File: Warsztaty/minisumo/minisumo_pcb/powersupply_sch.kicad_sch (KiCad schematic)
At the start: 7 parts, among them J1 Conn_01x02_Pin, U3 LM1117S-5.0, U8 LM1117S-3.3

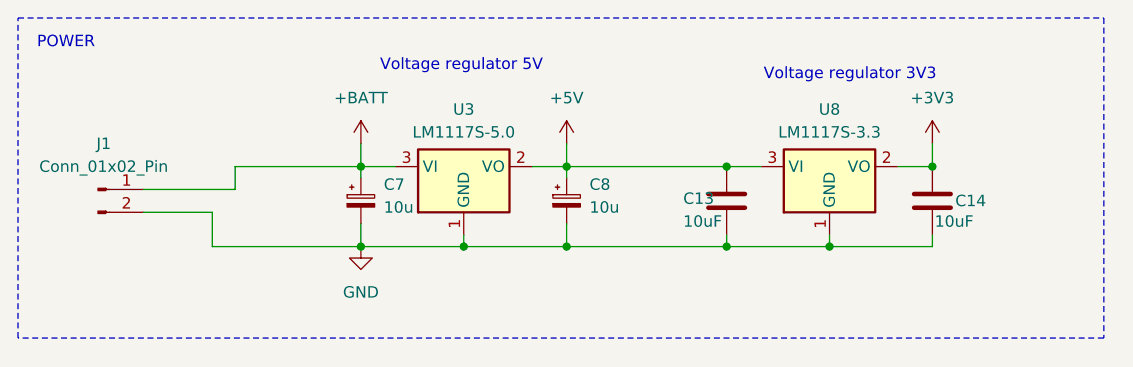
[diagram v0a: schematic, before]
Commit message: laczenie hierarchiczne schematu
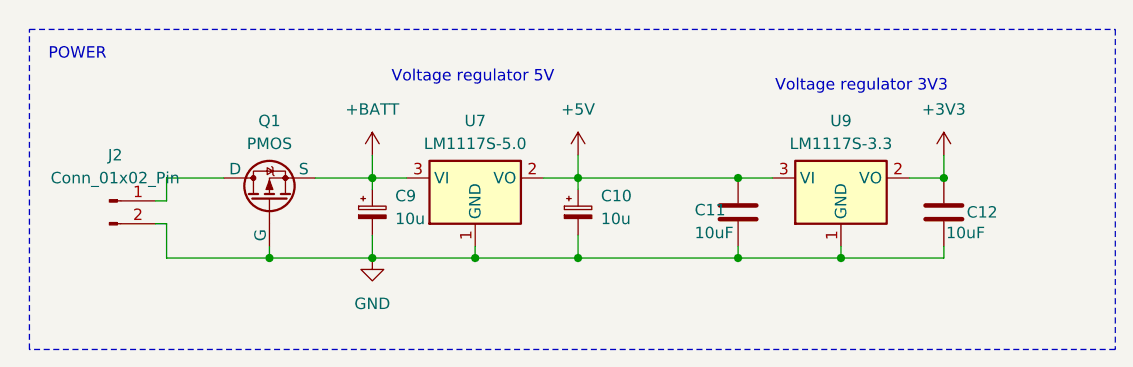
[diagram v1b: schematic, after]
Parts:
- removed C13, C14: 10uF, symbol Device:C
- removed C7, C8: 10u, symbol Device:C_Polarized_Small
- removed J1: Conn_01x02_Pin, symbol Connector:Conn_01x02_Pin
- removed U3: LM1117S-5.0, Package_TO_SOT_SMD:TO-263-3_TabPin2, symbol Regulator_Linear:LM1117S-5.0
- removed U8: LM1117S-3.3, Package_TO_SOT_SMD:TO-263-3_TabPin2, symbol Regulator_Linear:LM1117S-3.3
- added C10, C9: 10u, symbol Device:C_Polarized_Small
- added C11, C12: 10uF, symbol Device:C
- added J2: Conn_01x02_Pin, symbol Connector:Conn_01x02_Pin
- added Q1: PMOS, symbol Simulation_SPICE:PMOS
- added U7: LM1117S-5.0, Package_TO_SOT_SMD:TO-263-3_TabPin2, symbol Regulator_Linear:LM1117S-5.0
- added U9: LM1117S-3.3, Package_TO_SOT_SMD:TO-263-3_TabPin2, symbol Regulator_Linear:LM1117S-3.3
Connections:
- net +3V3: now also C12.1, U9.2 (VO)
- net +5V: now also C10.1, C11.1, U7.2 (VO), U9.3 (VI)
- net +BATT: now also C9.1, Q1.3 (S), U7.3 (VI)
- net GND: now also C10.2, C11.2, C12.2, C9.2, J2.2 (Pin_2), Q1.2 (G), U7.1 (GND), U9.1 (GND)
- new net: J2.1 (Pin_1), Q1.1 (D)

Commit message: wstepnie skonczony schemat
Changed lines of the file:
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@@
+		)
+	)
+	(hierarchical_label "+5V"
+		(shape input)
+		(at 74.93 29.21 0)
+		(fields_autoplaced yes)
+		(effects
+			(font
+				(size 1.27 1.27)
+			)
+			(justify left)
 		)
 	)

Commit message: chyba gotowy schemat
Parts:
- removed J2: Conn_01x02_Pin, symbol Connector:Conn_01x02_Pin
- added J1: HTSW-102-08-L-S, HTSW-102-08-L-S:SAMTEC_HTSW-102-08-L-S, symbol HTSW-102-08-L-S:HTSW-102-08-L-S
- C10, C11, C12, C9: footprint (none) -> Capacitor_SMD:C_0805_2012Metric_Pad1.18x1.45mm_HandSolder
- Q1: footprint (none) -> Package_TO_SOT_SMD:SOT-23-3
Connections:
- net GND: now also J1.01
- net +: now reaches Q1.1 (D)
- net +: now also J1.02
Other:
- moved on the sheet: C10, C11, C12, C9, Q1, U7, U9

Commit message: chyba gotowy schemat
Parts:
- removed C11, C12: 10uF, Capacitor_SMD:C_0805_2012Metric_Pad1.18x1.45mm_HandSolder, symbol Device:C
- removed U9: LM1117S-3.3, Package_TO_SOT_SMD:TO-263-3_TabPin2, symbol Regulator_Linear:LM1117S-3.3
- C10, C9: footprint Capacitor_SMD:C_0805_2012Metric_Pad1.18x1.45mm_HandSolder -> Capacitor_Tantalum_SMD:CP_EIA-3528-12_Kemet-T
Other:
- note removed: "Voltage regulator 3V3"

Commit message: stan przed usunięciem jednego czujnika lini
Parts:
- added S1: 1101M2S3CQE2, 1101M2S3CQE2:SW_1101M2S3CQE2, symbol 1101M2S3CQE2:1101M2S3CQE2
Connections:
- net +: now also S1.2; no longer Q1.1 (D)
- new net: Q1.1 (D), S1.1
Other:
- moved on the sheet: Q1
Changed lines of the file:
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@@
 	)
 	(junction
-		(at 43.18 40.64)
+		(at 45.72 40.64)
 		(diameter 0)
 		(color 0 0 0 0)
@@
 	(wire
 		(pts
-			(xy 43.18 39.37) (xy 43.18 40.64)
-		)
-		(stroke
-			(width 0)
-			(type default)
-		)
-	)
-	(wire
-		(pts
-			(xy 43.18 40.64) (xy 31.75 40.64)
+			(xy 45.72 39.37) (xy 45.72 40.64)
+		)
+		(stroke
+			(width 0)
+			(type default)
+		)
+	)
+	(wire
+		(pts
+			(xy 31.75 40.64) (xy 45.72 40.64)
 		)
 		(stroke
@@
 	(wire
 		(pts
-			(xy 31.75 31.75) (xy 38.1 31.75)
+			(xy 40.64 29.21) (xy 40.64 31.75)
+		)
+		(stroke
+			(width 0)
+			(type default)
+		)
+	)
+	(wire
+		(pts
+			(xy 45.72 40.64) (xy 54.61 40.64)
 		)
 		(stroke
@@
 	(wire
 		(pts
-			(xy 48.26 31.75) (xy 54.61 31.75)
-		)
-		(stroke
-			(width 0)
-			(type default)
-		)
-	)
-	(wire
-		(pts
-			(xy 43.18 40.64) (xy 54.61 40.64)
+			(xy 50.8 31.75) (xy 54.61 31.75)
 		)
 		(stroke
@@
 		(pts
 			(xy 73.66 31.75) (xy 77.47 31.75)
+		)
+		(stroke
+			(width 0)
+			(type default)
+		)
+	)
+	(wire
+		(pts
+			(xy 39.37 29.21) (xy 40.64 29.21)
 		)
 		(stroke
@@
 		(effects
 			(font
-				(size 1.27 1.27)
+				(size 0.762 0.762)
 			)
 			(justify left)
 		)
 		(property "Intersheetrefs" "${INTERSHEET_REFS}"
-			(at 31.75 27.1924 90)
+			(at 31.75 29.0152 90)
 			(effects
 				(font
@@
 		)
 		(property "Value" "HTSW-102-08-L-S"
-			(at 37.084 25.654 0)
+			(at 34.798 41.656 0)
 			(effects
 				(font
@@
 	(symbol
 		(lib_id "Simulation_SPICE:PMOS")
-		(at 43.18 34.29 90)
+		(at 45.72 34.29 90)
 		(unit 1)
 		(exclude_from_sim no)
@@
 		(fields_autoplaced yes)
 		(property "Reference" "Q1"
-			(at 43.18 25.4 90)
+			(at 45.72 25.4 90)
 			(effects
 				(font
@@
 		)
 		(property "Value" "PMOS"
-			(at 43.18 27.94 90)
+			(at 45.72 27.94 90)
 			(effects
 				(font
@@
 		)
 		(property "Footprint" "Package_TO_SOT_SMD:SOT-23-3"
-			(at 40.64 29.21 0)
+			(at 43.18 29.21 0)
 			(effects
 				(font
@@
 		)
 		(property "Datasheet" "https://ngspice.sourceforge.io/docs/ngspice-html-manual/manual.xhtml#cha_MOSFETs"
-			(at 55.88 34.29 0)
+			(at 58.42 34.29 0)
 			(effects
 				(font
@@
 		)
 		(property "Description" "P-MOSFET transistor, drain/source/gate"
-			(at 43.18 34.29 0)
+			(at 45.72 34.29 0)
 			(effects
 				(font
@@
 		)
 		(property "Sim.Device" "PMOS"
-			(at 60.325 34.29 0)
+			(at 62.865 34.29 0)
 			(effects
 				(font
@@
 		)
 		(property "Sim.Type" "VDMOS"
-			(at 62.23 34.29 0)
+			(at 64.77 34.29 0)
 			(effects
 				(font
@@
 		)
 		(property "Sim.Pins" "1=D 2=G 3=S"
-			(at 58.42 34.29 0)
+			(at 60.96 34.29 0)
 			(effects
 				(font
@@
 					(unit 1)
 				)
+			)
+		)
+	)
+	(symbol
+		(lib_id "1101M2S3CQE2:1101M2S3CQE2")
+		(at 34.29 31.75 0)
+		(unit 1)
+		(exclude_from_sim no)
+		(in_bom yes)
+		(on_board yes)
+		(dnp no)
+		(fields_autoplaced yes)
+		(property "Reference" "S1"
+			(at 35.56 26.67 0)
+			(effects
+				(font
+					(size 1.27 1.27)
+				)
+			)
+		)
+		(property "Value" "1101M2S3CQE2"
+			(at 35.56 26.67 0)
+			(effects
+				(font
+					(size 1.27 1.27)
+				)
+				(hide yes)
+			)
+		)
+		(property "Footprint" "1101M2S3CQE2:SW_1101M2S3CQE2"
+			(at 34.29 31.75 0)
+			(effects
+				(font
+					(size 1.27 1.27)
+				)
+				(justify bottom)
+				(hide yes)
+			)
+		)
+		(property "Datasheet" ""
+			(at 34.29 31.75 0)
+			(effects
+				(font
+					(size 1.27 1.27)
+				)
+				(hide yes)
+			)
+		)
+		(property "Description" ""
+			(at 34.29 31.75 0)
+			(effects
+				(font
+					(size 1.27 1.27)
+				)
+				(hide yes)
+			)
+		)
+		(property "MF" "C&K"
+			(at 34.29 31.75 0)
+			(effects
+				(font
+					(size 1.27 1.27)
+				)
+				(justify bottom)
+				(hide yes)
+			)
+		)
+		(property "Description_1" "\nSlide Switch SPDT Through Hole\n"
+			(at 34.29 31.75 0)
+			(effects
+				(font
+					(size 1.27 1.27)
+				)
+				(justify bottom)
+				(hide yes)
+			)
+		)
+		(property "Package" "None"
+			(at 34.29 31.75 0)
+			(effects
+				(font
+					(size 1.27 1.27)
+				)
+				(justify bottom)
+				(hide yes)
+			)
+		)
+		(property "Price" "None"
+			(at 34.29 31.75 0)
+			(effects
+				(font
+					(size 1.27 1.27)
+				)
+				(justify bottom)
+				(hide yes)
+			)
+		)
+		(property "Check_prices" "https://www.snapeda.com/parts/1101-M2S3CQE2/C%2526K/view-part/?ref=eda"
+			(at 34.29 31.75 0)
+			(effects
+				(font
+					(size 1.27 1.27)
+				)
+				(justify bottom)
+				(hide yes)
+			)
+		)
+		(property "SnapEDA_Link" "https://www.snapeda.com/parts/1101-M2S3CQE2/C%2526K/view-part/?ref=snap"
+			(at 34.29 31.75 0)
+			(effects
+				(font
+					(size 1.27 1.27)
+				)
+				(justify bottom)
+				(hide yes)
+			)
+		)
+		(property "MP" "1101-M2S3CQE2"
+			(at 34.29 31.75 0)
+			(effects
+				(font
+					(size 1.27 1.27)
+				)
+				(justify bottom)
+				(hide yes)
+			)
+		)
+		(property "Availability" "In Stock"
+			(at 34.29 31.75 0)
+			(effects
+				(font
+					(size 1.27 1.27)
+				)
+				(justify bottom)
+				(hide yes)
+			)
+		)
+		(property "MANUFACTURER" "CnK"
+			(at 34.29 31.75 0)
+			(effects
+				(font
+					(size 1.27 1.27)
+				)
+				(justify bottom)
+				(hide yes)
+			)
+		)
+		(pin "3"
+		)
+		(pin "2"
+		)
+		(pin "1"
+		)
+		(instances
+			(project "minisumo_pcb"
+				(path "/7b99a4ad-c15f-48f5-acdf-b2b295c8ee3b/fec592cb-397f-40c8-9127-e83f29739826"
+					(reference "S1")
+					(unit 1)
+				)

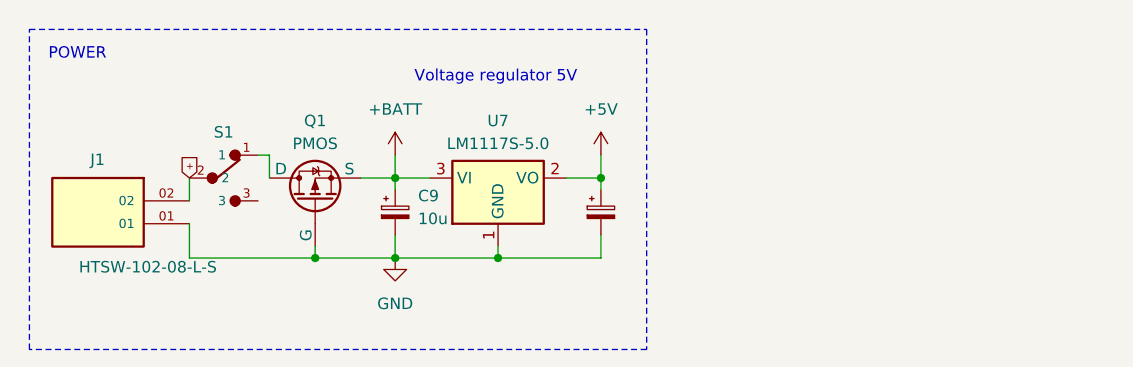
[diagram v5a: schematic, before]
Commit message: Wstępny wyglad robota i płytki
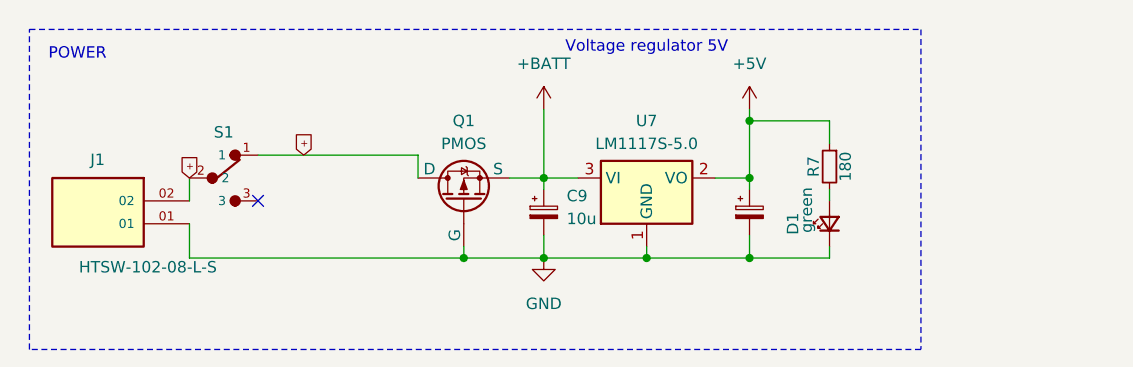
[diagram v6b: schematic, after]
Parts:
- added D1: green, LED_SMD:LED_0805_2012Metric, symbol Device:LED_Small
- added R7: 180, Resistor_SMD:R_0805_2012Metric, symbol Device:R_Small
- U7: footprint Package_TO_SOT_SMD:TO-263-3_TabPin2 -> Package_TO_SOT_SMD:SOT-223
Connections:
- net +: now also Q1.1 (D), S1.1
- net +5V: now also R7.1
- net GND: now also D1.1 (K)
- new net: D1.2 (A), R7.2
- no-connect marks 0 -> 1
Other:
- moved on the sheet: C9, Q1, U7

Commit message: koncowy projekt plytki i chyba model tez
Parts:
- renumbered D1 to +5V1, J1 to BATT1
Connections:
- net + renamed +IN
- net +IN: no longer Q1.1 (D), S1.1
- new net +OUT: Q1.1 (D), S1.1
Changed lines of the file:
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@@
 		)
 	)
-	(global_label "+"
+	(global_label "+OUT"
 		(shape input)
 		(at 44.45 29.21 90)
@@
 		)
 		(property "Intersheetrefs" "${INTERSHEET_REFS}"
-			(at 44.45 26.4752 90)
-			(effects
-				(font
-					(size 1.27 1.27)
-				)
-				(justify left)
-				(hide yes)
-			)
-		)
-	)
-	(global_label "+"
+			(at 44.45 24.298 90)
+			(effects
+				(font
+					(size 1.27 1.27)
+				)
+				(justify left)
+				(hide yes)
+			)
+		)
+	)
+	(global_label "+IN"
 		(shape input)
 		(at 31.75 31.75 90)
@@
 		)
 		(property "Intersheetrefs" "${INTERSHEET_REFS}"
-			(at 31.75 29.0152 90)
+			(at 31.75 27.854 90)
 			(effects
 				(font
@@
 		(on_board yes)
 		(dnp no)
-		(property "Reference" "J1"
+		(property "Reference" "BATT1"
 			(at 22.352 29.718 0)
 			(effects
@@
 			(project "minisumo_pcb"
 				(path "/7b99a4ad-c15f-48f5-acdf-b2b295c8ee3b/fec592cb-397f-40c8-9127-e83f29739826"
-					(reference "J1")
+					(reference "BATT1")
 					(unit 1)
 				)
@@
 				)
 				(justify left)
-				(hide yes)
 			)
 		)
@@
 				)
 				(justify left)
-				(hide yes)
 			)
 		)
@@
 		(on_board yes)
 		(dnp no)
-		(property "Reference" "D1"
+		(property "Reference" "+5V1"
 			(at 98.806 36.83 0)
 			(effects
@@
 			(project "minisumo_pcb"
 				(path "/7b99a4ad-c15f-48f5-acdf-b2b295c8ee3b/fec592cb-397f-40c8-9127-e83f29739826"
-					(reference "D1")
+					(reference "+5V1")
 					(unit 1)
 				)
@@
 		(lib_id "Device:C_Polarized_Small")
 		(at 71.12 35.56 0)
-		(unit 1)
-		(exclude_from_sim no)
-		(in_bom yes)
-		(on_board yes)
-		(dnp no)
-		(fields_autoplaced yes)
+		(mirror y)
+		(unit 1)
+		(exclude_from_sim no)
+		(in_bom yes)
+		(on_board yes)
+		(dnp no)
 		(property "Reference" "C9"
-			(at 73.66 33.7438 0)
+			(at 68.58 33.7438 0)
 			(effects
 				(font
@@
 		)
 		(property "Value" "10u"
-			(at 73.66 36.2838 0)
-			(effects
-				(font
+			(at 68.58 36.2838 0)
+			(effects
+				(font
